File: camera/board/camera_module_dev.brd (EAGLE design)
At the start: 160 x 100 mm, 11 parts, among them IC1 74541PW, IC2 74541PW, Q1 MOSFET-NCHANNELBSS123LT1G, Q2 MOSFET-NCHANNELBSS123LT1G

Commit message: Schematic more or less done, moving to layout
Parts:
- added C1: 2.2uF, biomimetic:0402-CAP
- added C10, C11, C12, C7: 1uF, biomimetic:0603-CAP
- added C13, C14, C15, C16, C5, C6, C8, C9: 100nF, biomimetic:0402-CAP
- added C2, C3: 1uF, biomimetic:0402-CAP
- added C4: 10nF, biomimetic:0402-CAP
- added JP3, JP4: (no value), pinhead:1X09
- added L1, L2: 3.3uH, biomimetic:1007
- added R1: 18k, biomimetic:0402-RES
- added R10, R11, R8, R9: 4k7, biomimetic:0402-RES
- added R2: 18k/5k, biomimetic:0402-RES
- added R3, R4, R7: 10k, biomimetic:0402-RES
- added R5: (no value), biomimetic:0402-RES
- added R6: 1k8, biomimetic:0402-RES
- added SJ1, SJ10, SJ11, SJ2, SJ3, SJ4, SJ5, SJ6, SJ7, SJ8, SJ9: SOLDERJUMPERNO, SparkFun-Passives:SJ_2S-NO
- added SJ12, SJ13, SJ14: (no value), SparkFun-Passives:SJ_3
- moved U$4 74.5 mm to (-97.8, -11.4)
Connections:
- removed net AVDD: U$1.A2, U$2.1, U$3.A9
- removed net V+: U$6.2
- removed net VCC: IC1.20, IC2.20
- removed net VSS: QG1.2
- new net +3V3: C1.1, C5.2, C6.2, IC1.20, IC2.20, R11.1, R5.1, R9.1, SJ12.3, SJ13.3, U$3.A9, U$4.11, U$6.2
- new net D0: IC1.2, SJ1.2, U$1.B3, U$2.11, U$3.B9
- new net D1: IC1.3, SJ2.2, U$1.B4, U$2.12, U$3.B10
- new net D2: IC1.4, SJ3.2, U$1.C4, U$2.13, U$3.B11
- new net D3: IC1.5, SJ4.2, U$1.D4, U$2.14, U$3.B12
- new net D4: IC1.6, SJ5.2, U$1.E3, U$2.17, U$3.B13
- new net D5: IC1.7, SJ6.2, U$1.D3, U$2.18, U$3.B14
- new net D6: IC1.8, SJ7.2, U$1.E2, U$2.19, U$3.B15
- new net D7: IC1.9, SJ8.2, U$1.E1, U$2.20, U$3.B16
- new net HSYNC: IC2.4, SJ11.2, U$1.C1, U$2.9, U$3.A4
- new net N$1: QG1.3, SJ14.3
- new net N$10: IC2.1, SJ12.2
- new net N$19: R1.2, R4.1, U$6.8
- new net N$2: JP3.8, U$4.8
- new net N$21: R2.2, R3.1, U$6.4
- new net N$3: R6.1, R7.2, SJ14.1
- new net N$4: C13.1, U$1.A3
- new net N$5: C9.1, U$1.A4
- new net N$6: C12.1, C14.2, C16.1, C7.2, L2.2, U$1.A2, U$2.6
- new net N$7: IC1.1, SJ13.2
- new net N$8: C10.1, C11.2, C15.2, C8.1, L1.2, U$1.E4, U$2.1, U$2.16
- new net PCLK: IC2.2, SJ9.2, U$1.D1, U$2.10, U$3.A6
- new net PMOD_D0: IC1.18, JP4.1, SJ1.1, U$5.1
- new net PMOD_D1: IC1.17, JP4.2, SJ2.1, U$5.3
- new net PMOD_D2: IC1.16, JP4.3, SJ3.1, U$5.5
- new net PMOD_D3: IC1.15, JP4.4, SJ4.1, U$5.7
- new net PMOD_D4: IC1.14, JP4.5, SJ5.1, U$5.2
- new net PMOD_D5: IC1.13, JP4.6, SJ6.1, U$5.4
- new net PMOD_D6: IC1.11, IC1.12, JP4.7, SJ7.1, SJ8.1, U$5.6
- new net PMOD_D7: JP4.8, U$5.8
- new net PMOD_HSYNC: IC2.16, JP3.7, SJ11.1, U$4.6
- new net PMOD_PCLK: IC2.18, JP3.5, SJ9.1, U$4.2
- new net PMOD_RESET: IC1.19, IC2.19, JP3.1, QG1.1, R5.2, U$1.A1, U$2.3, U$3.A1, U$4.1, U$6.6
- new net PMOD_SCL: JP3.3, Q2.3, R9.2, U$4.5
- new net PMOD_SDA: JP3.4, Q1.3, R11.2, U$4.7
- new net PMOD_VSYNC: IC2.17, JP3.6, SJ10.1, U$4.4
- new net PMOD_XCLK: JP3.2, R6.2, U$4.3
- new net SCL: Q2.2, R8.2, U$1.B2, U$2.4, U$3.A3
- new net SDA: Q1.2, R10.2, U$1.B1, U$2.5, U$3.A2
- new net VCCIO: C2.1, C4.2, L1.1, Q1.1, Q2.1, QG1.4, R1.1, R10.1, R8.1, U$6.1
- new net VSYNC: IC2.3, SJ10.2, U$1.C2, U$2.8, U$3.A5
- new net XCLK: SJ14.2, U$1.D2, U$2.2, U$3.A7
- net DVDD: no longer U$1.E4, U$2.6
- net GND: now also C1.2, C10.2, C11.1, C12.2, C13.2, C14.1, C15.1, C16.2, C2.2, C3.2, C4.1, C5.1, C6.1, C7.1, C8.2, C9.2, IC2.5, IC2.6, IC2.7, IC2.8, IC2.9, JP3.9, JP4.9, QG1.2, R3.2, R4.2, R7.1, SJ12.1, SJ13.1, U$2.15, U$4.10, U$5.10
- net V: no longer U$1.A3, U$1.A4, U$2.15, U$2.16
- net VDD: now also C3.1, L2.1, R2.1, U$6.3; no longer QG1.4

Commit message: Pmod signal routing more or less done
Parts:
- C10, C11, C12, C7: value 1uF -> 4.7uF
- moved C14 207.3 mm to (30.0, 25.4), flipped to the bottom, turned to 270 degrees
- moved C13 203.9 mm to (28.7, 25.4), flipped to the bottom, turned to 90 degrees
- moved C16 202.9 mm to (12.0, 29.3), flipped to the bottom, turned to 180 degrees
- moved C15 202.8 mm to (17.1, 28.2), flipped to the bottom
- moved C10 198.6 mm to (27.3, 29.6), flipped to the bottom, turned to 270 degrees
- moved C8 194.8 mm to (28.8, 29.1), flipped to the bottom, turned to 270 degrees
- moved C11 193.7 mm to (17.0, 29.7), flipped to the bottom
- moved C12 193.6 mm to (12.1, 30.8), flipped to the bottom, turned to 180 degrees
- moved C9 193.6 mm to (27.4, 25.4), flipped to the bottom, turned to 90 degrees
- moved C7 192.6 mm to (31.5, 25.9), flipped to the bottom, turned to 270 degrees
- moved R5 181.1 mm to (27.6, 48.6), turned to 180 degrees
- moved R10 179.4 mm to (25.8, 18.6), turned to 180 degrees
- moved R4 178.4 mm to (25.7, 50.4)
- moved R11 177.6 mm to (25.3, 12.6)
- moved C5 175.5 mm to (38.7, 14.1), turned to 180 degrees
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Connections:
- net PMOD_D6: no longer IC1.11, SJ8.1
- net PMOD_D7: now also IC1.11, SJ8.1
- net PMOD_SCL: now also JP3.4, U$4.7; no longer JP3.3, U$4.5
- net PMOD_SDA: now also JP3.2, U$4.3; no longer JP3.4, U$4.7
- net PMOD_XCLK: now also JP3.3, U$4.5; no longer JP3.2, U$4.3
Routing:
- net +3V3: track 0.00 -> 50.4 mm, vias 0 -> 4
- net PMOD_RESET: track 0.00 -> 39.7 mm, vias 0 -> 2
- net PMOD_D1: track 0.00 -> 21.3 mm
- net PMOD_D0: track 0.00 -> 21.1 mm
- net PMOD_D7: track 0.00 -> 19.7 mm
- net PMOD_SCL: track 0.00 -> 19.4 mm
- net PMOD_D5: track 0.00 -> 19.2 mm
- net PMOD_HSYNC: track 0.00 -> 19.2 mm
- net PMOD_D4: track 0.00 -> 18.4 mm
- net PMOD_D2: track 0.00 -> 17.3 mm
- net PMOD_D3: track 0.00 -> 17.2 mm
- net PMOD_PCLK: track 0.00 -> 17.2 mm
- net PMOD_D6: track 0.00 -> 16.9 mm
- net PMOD_VSYNC: track 0.00 -> 16.3 mm
- net PMOD_SDA: track 0.00 -> 14.9 mm
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- added copper zone on layer 1, net GND
- added copper zone on layer 16, net GND
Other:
- board size 160 x 100 mm -> 48.3 x 38.1 mm

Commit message: Most layout done
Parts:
- moved C1 34.5 mm to (26.4, 14.4), flipped to the bottom, turned to 0 degrees
- moved R5 34.2 mm to (28.8, 14.4), flipped to the bottom
- moved C2 33.8 mm to (25.7, 16.8), flipped to the bottom, turned to 90 degrees
- moved R4 33.6 mm to (24.4, 16.8), flipped to the bottom, turned to 90 degrees
- moved R1 33.6 mm to (23.1, 16.8), flipped to the bottom, turned to 90 degrees
- moved C4 33.0 mm to (15.6, 15.6), turned to 90 degrees
- moved U$6 31.9 mm to (27.6, 16.8), flipped to the bottom, turned to 90 degrees
- moved R2 31.2 mm to (32.1, 16.8), flipped to the bottom, turned to 90 degrees
- moved QG1 31.1 mm to (13.2, 15.6), turned to 0 degrees
- moved C3 30.9 mm to (29.5, 16.8), flipped to the bottom
- moved R3 30.4 mm to (30.8, 16.8), flipped to the bottom, turned to 90 degrees
- moved R7 28.7 mm to (16.2, 18.7), turned to 0 degrees
- moved R6 28.1 mm to (16.2, 17.4)
- moved SJ14 25.6 mm to (13.2, 18.1)
- moved L2 14.6 mm to (34.2, 16.8)
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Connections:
- removed net DVDD: U$3.A16
- new net AVDD: U$3.A9
- net +3V3: now also U$3.A16; no longer U$3.A9
- net N$19: now also U$6.4; no longer U$6.8
- net N$21: now also U$6.8; no longer U$6.4
- net VCCIO: now also U$6.3; no longer U$6.1
- net VDD: now also U$6.1; no longer U$6.3
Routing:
- net D0: track 3.59 -> 78.4 mm, vias 0 -> 4
- net D1: track 1.68 -> 73.3 mm, vias 0 -> 3
- net D2: track 3.38 -> 72.2 mm, vias 0 -> 3
- net PMOD_RESET: track 39.7 -> 104.9 mm, vias 2 -> 6
- net XCLK: track 0.00 -> 63.7 mm
- net D3: track 1.66 -> 63.2 mm, vias 0 -> 4
- net SCL: track 2.14 -> 63.4 mm, vias 0 -> 2
- net VSYNC: track 3.54 -> 60.5 mm, vias 0 -> 1
- net D7: track 2.08 -> 56.6 mm, vias 0 -> 3
- net D5: track 1.87 -> 56.3 mm, vias 0 -> 4
- net D4: track 3.56 -> 57.9 mm, vias 0 -> 4
- net SDA: track 2.09 -> 55.9 mm, vias 0 -> 2
- net HSYNC: track 1.85 -> 55.6 mm, vias 0 -> 2
- net N$6: track 0.00 -> 51.9 mm, vias 0 -> 5
- net PCLK: track 1.64 -> 53.0 mm, vias 0 -> 2
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
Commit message: Layout done
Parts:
- moved C16 1.63 mm to (9.30, 31.9)
- moved C12 1.20 mm to (10.5, 31.4)
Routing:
- net N$6: track 51.9 -> 45.5 mm, vias 5 -> 4
- net D0: track 78.4 -> 74.2 mm, vias 4 -> 1
- net D7: track 56.6 -> 52.9 mm
- net SCL: track 63.4 -> 60.6 mm
- net D2: track 72.2 -> 69.6 mm
- net V: track 0.00 -> 2.54 mm
- net D1: track 73.3 -> 71.6 mm
- net N$8: track 41.5 -> 39.9 mm
- net VCCIO: track 24.8 -> 25.6 mm
- net D6: track 55.4 -> 55.8 mm, vias 4 -> 3
- net D5: track 56.3 -> 56.4 mm, vias 4 -> 5
- net D4: vias 4 -> 3
- net D3: vias 4 -> 3

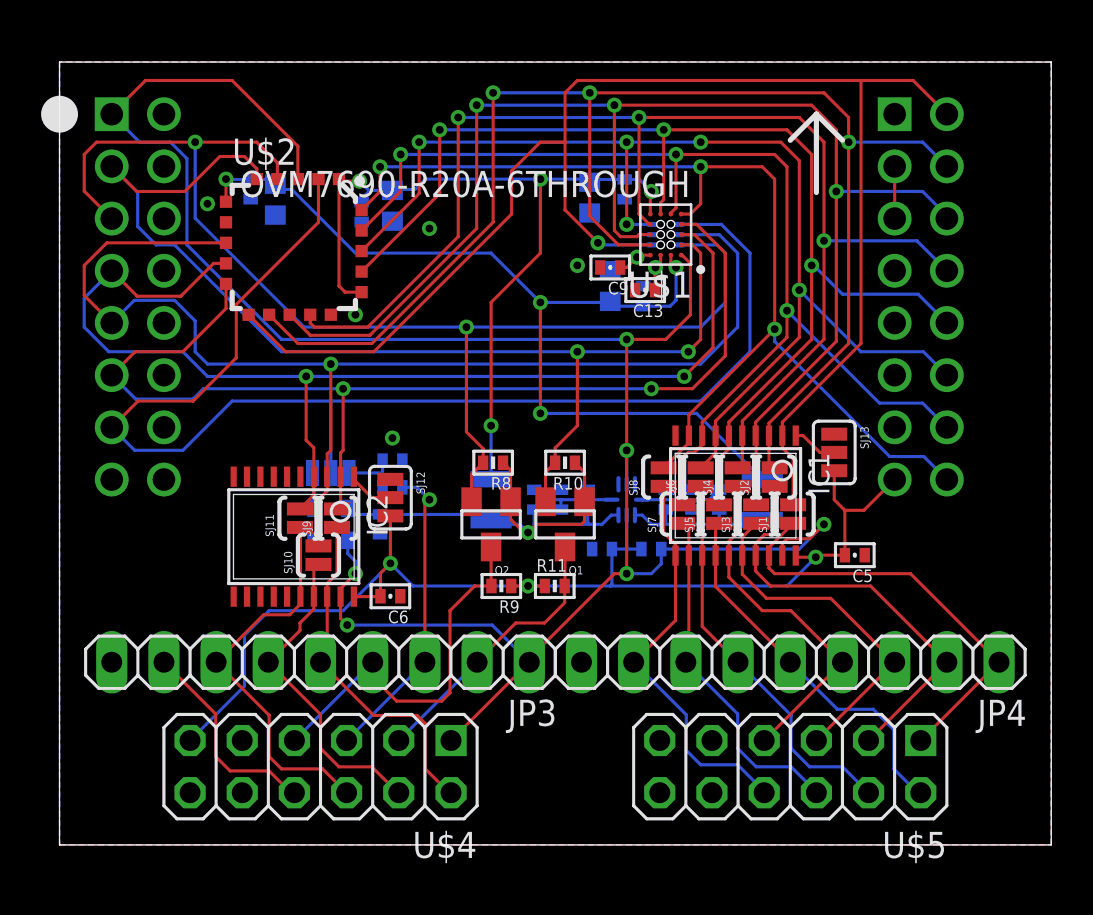
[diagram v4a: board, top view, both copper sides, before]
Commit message: Fixing small things preparing for panelization
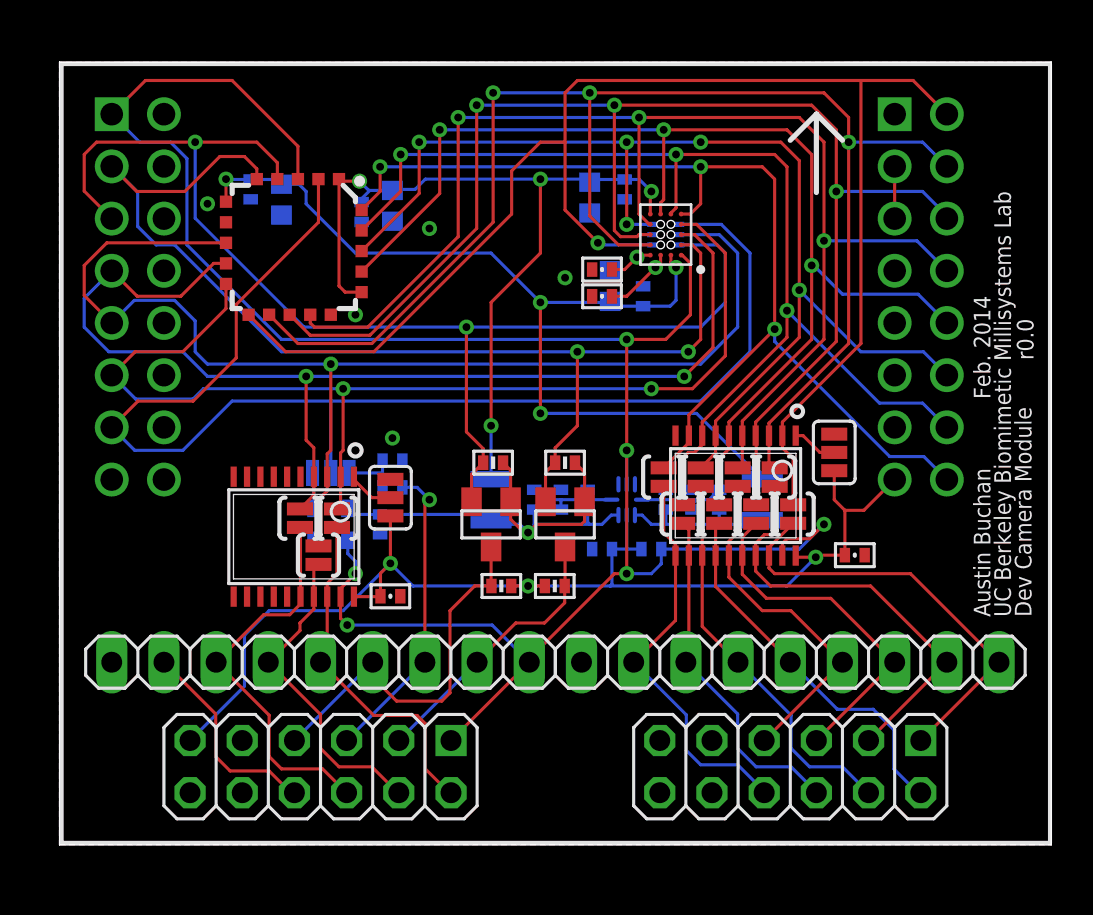
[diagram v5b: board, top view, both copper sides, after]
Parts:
- added U$7: INFO, modular_robotics:INFO
- moved C13 2.12 mm to (26.4, 26.7)
- moved C9 0.41 mm to (26.4, 28.0)
- moved C12 0.30 mm to (10.8, 31.4)
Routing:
- net N$4: track 1.81 -> 3.43 mm
